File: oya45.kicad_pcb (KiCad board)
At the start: 2 copper layers, 94 parts, among them U1 Elite-C

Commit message: added pro micro
pro micro instead of elite c for less pads
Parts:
- U1: value Elite-C -> ProMicro; footprint Keebio-Parts:Elite-C -> Keebio-Parts:ArduinoProMicro
- moved U1 1.59 mm to (218.3, 38.1)
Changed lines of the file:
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@@
     (zones 0)
     (modules 94)
-    (nets 75)
+    (nets 70)
   )
   (page A4)
@@
   (net 68 "Net-(U1-Pad2)")
   (net 69 "Net-(U1-Pad1)")
-  (net 70 "Net-(U1-Pad25)")
-  (net 71 "Net-(U1-Pad26)")
-  (net 72 "Net-(U1-Pad27)")
-  (net 73 "Net-(U1-Pad28)")
-  (net 74 "Net-(U1-Pad29)")
   (net_class Default "This is the default net class."
     (clearance 0.00508)
@@
     (add_net "Net-(U1-Pad23)")
     (add_net "Net-(U1-Pad24)")
-    (add_net "Net-(U1-Pad25)")
-    (add_net "Net-(U1-Pad26)")
-    (add_net "Net-(U1-Pad27)")
-    (add_net "Net-(U1-Pad28)")
-    (add_net "Net-(U1-Pad29)")
     (add_net "Net-(U1-Pad3)")
     (add_net "Net-(U1-Pad4)")
@@
     (add_net row4)
   )
-  (module Keebio-Parts:Elite-C (layer F.Cu)
-    (at 219.86875 38.1 180)
+  (module Keebio-Parts:ArduinoProMicro (layer F.Cu)
+    (at 218.28125 38.1 180)
     (fp_text reference U1 (at 0 1.625) (layer F.SilkS) hide
-      (effects (font (size 1.2 1.2) (thickness 0.2032)))
-    )
-    (fp_text value Elite-C (at 0 0) (layer F.SilkS) hide
-      (effects (font (size 1.2 1.2) (thickness 0.2032)))
-    )
-    (fp_text user D5 (at 12.4 2.54 90) (layer B.SilkS)
-      (effects (font (size 0.8 0.8) (thickness 0.15)) (justify mirror))
-    )
-    (fp_text user D5 (at 12.4 2.54 90) (layer F.SilkS)
-      (effects (font (size 0.8 0.8) (thickness 0.15)))
-    )
-    (fp_text user F1 (at 12.4 -2.54 90) (layer F.SilkS)
-      (effects (font (size 0.8 0.8) (thickness 0.15)))
-    )
-    (fp_text user F1 (at 12.4 -2.54 90) (layer B.SilkS)
-      (effects (font (size 0.8 0.8) (thickness 0.15)) (justify mirror))
-    )
-    (fp_text user C7 (at 12.4 0 90) (layer B.SilkS)
-      (effects (font (size 0.8 0.8) (thickness 0.15)) (justify mirror))
-    )
-    (fp_text user C7 (at 12.4 0 90) (layer F.SilkS)
-      (effects (font (size 0.8 0.8) (thickness 0.15)))
-    )
-    (fp_text user B6 (at 12.7 -6.4 315 unlocked) (layer B.SilkS)
-      (effects (font (size 0.7 0.7) (thickness 0.15)) (justify mirror))
-    )
-    (fp_text user B6 (at 12.7 -6.4 315 unlocked) (layer F.SilkS)
-      (effects (font (size 0.7 0.7) (thickness 0.15)))
-    )
-    (fp_text user F0 (at 12.6 -4.5 90) (layer F.SilkS)
-      (effects (font (size 0.7 0.7) (thickness 0.15)))
-    )
-    (fp_text user F0 (at 12.6 -4.5 90) (layer B.SilkS)
-      (effects (font (size 0.7 0.7) (thickness 0.15)) (justify mirror))
-    )
-    (fp_text user B7 (at 12.6 4.5 90) (layer B.SilkS)
-      (effects (font (size 0.7 0.7) (thickness 0.15)) (justify mirror))
-    )
-    (fp_text user B7 (at 12.6 4.5 90) (layer F.SilkS)
-      (effects (font (size 0.7 0.7) (thickness 0.15)))
+      (effects (font (size 1.27 1.524) (thickness 0.2032)))
+    )
+    (fp_text value ProMicro (at 0 0) (layer F.SilkS) hide
+      (effects (font (size 1.27 1.524) (thickness 0.2032)))
     )
     (fp_line (start -15.24 6.35) (end -15.24 8.89) (layer F.SilkS) (width 0.381))
@@
       (effects (font (size 0.8 0.8) (thickness 0.15)))
     )
-    (fp_text user B5 (at 12.7 6.4 45) (layer F.SilkS)
-      (effects (font (size 0.7 0.7) (thickness 0.15)))
+    (fp_text user B5 (at 13.97 5.461 90) (layer F.SilkS)
+      (effects (font (size 0.8 0.8) (thickness 0.15)))
+    )
+    (fp_text user B6 (at 13.97 -5.461 90) (layer F.SilkS)
+      (effects (font (size 0.8 0.8) (thickness 0.15)))
     )
     (fp_text user B2 (at 11.43 -5.461 90) (layer B.SilkS)
@@
       (effects (font (size 0.8 0.8) (thickness 0.15)))
     )
-    (fp_text user B0 (at -13.97 -5.461 90) (layer F.SilkS)
-      (effects (font (size 0.8 0.8) (thickness 0.15)))
-    )
-    (fp_text user B0 (at -13.97 -5.461 90) (layer B.SilkS)
+    (fp_text user RAW (at -13.97 -5.461 90) (layer F.SilkS)
+      (effects (font (size 0.8 0.8) (thickness 0.15)))
+    )
+    (fp_text user RAW (at -13.97 -5.461 90) (layer B.SilkS)
       (effects (font (size 0.8 0.8) (thickness 0.15)) (justify mirror))
     )
@@
       (effects (font (size 0.8 0.8) (thickness 0.15)))
     )
-    (fp_text user B5 (at 12.7 6.4 45) (layer B.SilkS)
-      (effects (font (size 0.7 0.7) (thickness 0.15)) (justify mirror))
+    (fp_text user B6 (at 13.97 -5.461 90) (layer B.SilkS)
+      (effects (font (size 0.8 0.8) (thickness 0.15)) (justify mirror))
+    )
+    (fp_text user B5 (at 13.97 5.461 90) (layer B.SilkS)
+      (effects (font (size 0.8 0.8) (thickness 0.15)) (justify mirror))
     )
     (fp_text user B4 (at 11.43 5.461 90) (layer B.SilkS)
@@
     (fp_line (start -15.24 6.35) (end -12.7 6.35) (layer B.SilkS) (width 0.381))
     (fp_line (start -12.7 6.35) (end -12.7 8.89) (layer B.SilkS) (width 0.381))
-    (pad 25 thru_hole circle (at 13.97 5.08 180) (size 1.7526 1.7526) (drill 1.0922) (layers *.Cu *.SilkS *.Mask)
-      (net 70 "Net-(U1-Pad25)"))
-    (pad 26 thru_hole circle (at 13.97 2.54 180) (size 1.7526 1.7526) (drill 1.0922) (layers *.Cu *.SilkS *.Mask)
-      (net 71 "Net-(U1-Pad26)"))
-    (pad 27 thru_hole circle (at 13.97 0 180) (size 1.7526 1.7526) (drill 1.0922) (layers *.Cu *.SilkS *.Mask)
-      (net 72 "Net-(U1-Pad27)"))
-    (pad 28 thru_hole circle (at 13.97 -2.54 180) (size 1.7526 1.7526) (drill 1.0922) (layers *.Cu *.SilkS *.Mask)
-      (net 73 "Net-(U1-Pad28)"))
-    (pad 29 thru_hole circle (at 13.97 -5.08 180) (size 1.7526 1.7526) (drill 1.0922) (layers *.Cu *.SilkS *.Mask)
-      (net 74 "Net-(U1-Pad29)"))
     (pad 24 thru_hole circle (at -13.97 -7.62 180) (size 1.7526 1.7526) (drill 1.0922) (layers *.Cu *.SilkS *.Mask)
       (net 61 "Net-(U1-Pad24)"))
-    (pad 12 thru_hole circle (at 13.97 7.3914 180) (size 1.7526 1.7526) (drill 1.0922) (layers *.Cu *.SilkS *.Mask)
+    (pad 12 thru_hole circle (at 13.97 7.62 180) (size 1.7526 1.7526) (drill 1.0922) (layers *.Cu *.SilkS *.Mask)
       (net 53 col2))
     (pad 23 thru_hole circle (at -11.43 -7.62 180) (size 1.7526 1.7526) (drill 1.0922) (layers *.Cu *.SilkS *.Mask)

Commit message: added fillets
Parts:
- moved U1 43.9 mm to (208.8, -4.76)
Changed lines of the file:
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@@
   (general
     (thickness 1.6)
-    (drawings 0)
+    (drawings 6)
     (tracks 0)
     (zones 0)
@@
   )
   (module Keebio-Parts:ArduinoProMicro (layer F.Cu)
-    (at 218.28125 38.1 180)
+    (at 208.75625 -4.7625 180)
     (fp_text reference U1 (at 0 1.625) (layer F.SilkS) hide
       (effects (font (size 1.27 1.524) (thickness 0.2032)))
@@
       (net 1 row1))
   )
+  (gr_arc (start 150.01875 30.95625) (end 152.4 30.95625) (angle -90) (layer F.SilkS) (width 0.12))
+  (gr_arc (start 235.74375 50.00625) (end 238.125 50.00625) (angle -90) (layer F.SilkS) (width 0.12))
+  (gr_arc (start 235.74375 121.44375) (end 235.74375 123.825) (angle -90) (layer F.SilkS) (width 0.12))
+  (gr_arc (start 50.00625 121.44375) (end 47.625 121.44375) (angle -90) (layer F.SilkS) (width 0.12))
+  (gr_arc (start 50.00625 50.00625) (end 50.00625 47.625) (angle -90) (layer F.SilkS) (width 0.12))
+  (gr_arc (start 59.53125 30.95625) (end 59.53125 28.575) (angle -90) (layer F.SilkS) (width 0.12))
 )

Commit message: column tracing
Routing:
- net col4: track 0.00 -> 100.1 mm
- net col3: track 0.00 -> 80.1 mm
- net col2: track 0.00 -> 80.1 mm
- net col1: track 0.00 -> 80.1 mm
- net col5: track 0.00 -> 66.7 mm
- net col0: track 0.00 -> 61.1 mm
- net col6: track 0.00 -> 58.1 mm
- net col9: track 0.00 -> 57.2 mm
- net col8: track 0.00 -> 57.2 mm
- net col7: track 0.00 -> 57.2 mm
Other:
- net class Default: clearance 0.00508 -> 0.2; trace_width 0.00508 -> 0.254
- rule trace_clearance: 0.00508 -> 0.2
- rule trace_min: 0.00381 -> 0.2
- rule via_min_drill: 0.00762 -> 0.3
- rule via_min_size: 0.00381 -> 0.4
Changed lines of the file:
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@@
     (thickness 1.6)
     (drawings 6)
-    (tracks 0)
+    (tracks 31)
     (zones 0)
     (modules 94)
@@
   )
   (setup
-    (last_trace_width 0.00508)
-    (trace_clearance 0.00508)
+    (last_trace_width 0.254)
+    (trace_clearance 0.2)
     (zone_clearance 0.508)
     (zone_45_only no)
-    (trace_min 0.00381)
+    (trace_min 0.2)
     (via_size 0.8)
     (via_drill 0.4)
-    (via_min_size 0.00381)
-    (via_min_drill 0.00762)
+    (via_min_size 0.4)
+    (via_min_drill 0.3)
     (uvia_size 0.3)
     (uvia_drill 0.1)
     (uvias_allowed no)
-    (uvia_min_size 0.00381)
-    (uvia_min_drill 0.00254)
+    (uvia_min_size 0.2)
+    (uvia_min_drill 0.1)
     (edge_width 0.05)
     (segment_width 0.2)
@@
   (net 69 "Net-(U1-Pad1)")
   (net_class Default "This is the default net class."
-    (clearance 0.00508)
-    (trace_width 0.00508)
+    (clearance 0.2)
+    (trace_width 0.254)
     (via_dia 0.8)
     (via_drill 0.4)
@@
   (gr_arc (start 50.00625 50.00625) (end 50.00625 47.625) (angle -90) (layer F.SilkS) (width 0.12))
   (gr_arc (start 59.53125 30.95625) (end 59.53125 28.575) (angle -90) (layer F.SilkS) (width 0.12))
+  (segment (start 70.485 45.085) (end 60.96 54.61) (width 0.254) (layer F.Cu) (net 51))
+  (segment (start 70.485 35.56) (end 70.485 45.085) (width 0.254) (layer F.Cu) (net 51))
+  (segment (start 60.96 54.61) (end 60.96 92.71) (width 0.254) (layer F.Cu) (net 51))
+  (segment (start 89.535 45.085) (end 80.01 54.61) (width 0.254) (layer F.Cu) (net 52))
+  (segment (start 89.535 35.56) (end 89.535 45.085) (width 0.254) (layer F.Cu) (net 52))
+  (segment (start 80.01 54.61) (end 80.01 111.76) (width 0.254) (layer F.Cu) (net 52))
+  (segment (start 108.585 45.085) (end 99.06 54.61) (width 0.254) (layer F.Cu) (net 53))
+  (segment (start 108.585 35.56) (end 108.585 45.085) (width 0.254) (layer F.Cu) (net 53))
+  (segment (start 99.06 54.61) (end 99.06 111.76) (width 0.254) (layer F.Cu) (net 53))
+  (segment (start 127.635 45.085) (end 118.11 54.61) (width 0.254) (layer F.Cu) (net 54))
+  (segment (start 127.635 35.56) (end 127.635 45.085) (width 0.254) (layer F.Cu) (net 54))
+  (segment (start 118.11 54.61) (end 118.11 111.76) (width 0.254) (layer F.Cu) (net 54))
+  (segment (start 146.685 45.085) (end 137.16 54.61) (width 0.254) (layer F.Cu) (net 55))
+  (segment (start 146.685 35.56) (end 146.685 45.085) (width 0.254) (layer F.Cu) (net 55))
+  (segment (start 137.16 54.61) (end 137.16 103.02875) (width 0.254) (layer F.Cu) (net 55))
+  (segment (start 138.284999 110.635001) (end 137.16 111.76) (width 0.254) (layer F.Cu) (net 55))
+  (segment (start 138.284999 104.153749) (end 138.284999 110.635001) (width 0.254) (layer F.Cu) (net 55))
+  (segment (start 137.16 103.02875) (end 138.284999 104.153749) (width 0.254) (layer F.Cu) (net 55))
+  (segment (start 138.75099 111.76) (end 146.685 111.76) (width 0.254) (layer B.Cu) (net 55))
+  (segment (start 137.16 111.76) (end 138.75099 111.76) (width 0.254) (layer B.Cu) (net 55))
+  (segment (start 137.16 111.76) (end 127.635 111.76) (width 0.254) (layer B.Cu) (net 55))
+  (segment (start 156.21 54.61) (end 156.21 111.76) (width 0.254) (layer F.Cu) (net 56))
+  (segment (start 157.80099 111.76) (end 165.735 111.76) (width 0.254) (layer F.Cu) (net 56))
+  (segment (start 156.21 111.76) (end 157.80099 111.76) (width 0.254) (layer F.Cu) (net 56))
+  (segment (start 175.26 54.61) (end 175.26 103.02875) (width 0.254) (layer F.Cu) (net 57))
+  (segment (start 176.384999 110.635001) (end 175.26 111.76) (width 0.254) (layer F.Cu) (net 57))
+  (segment (start 176.384999 104.153749) (end 176.384999 110.635001) (width 0.254) (layer F.Cu) (net 57))
+  (segment (start 175.26 103.02875) (end 176.384999 104.153749) (width 0.254) (layer F.Cu) (net 57))
+  (segment (start 194.31 54.61) (end 194.31 111.76) (width 0.254) (layer F.Cu) (net 58))
+  (segment (start 213.36 54.61) (end 213.36 111.76) (width 0.254) (layer F.Cu) (net 59))
+  (segment (start 232.41 54.61) (end 232.41 111.76) (width 0.254) (layer F.Cu) (net 60))
 )

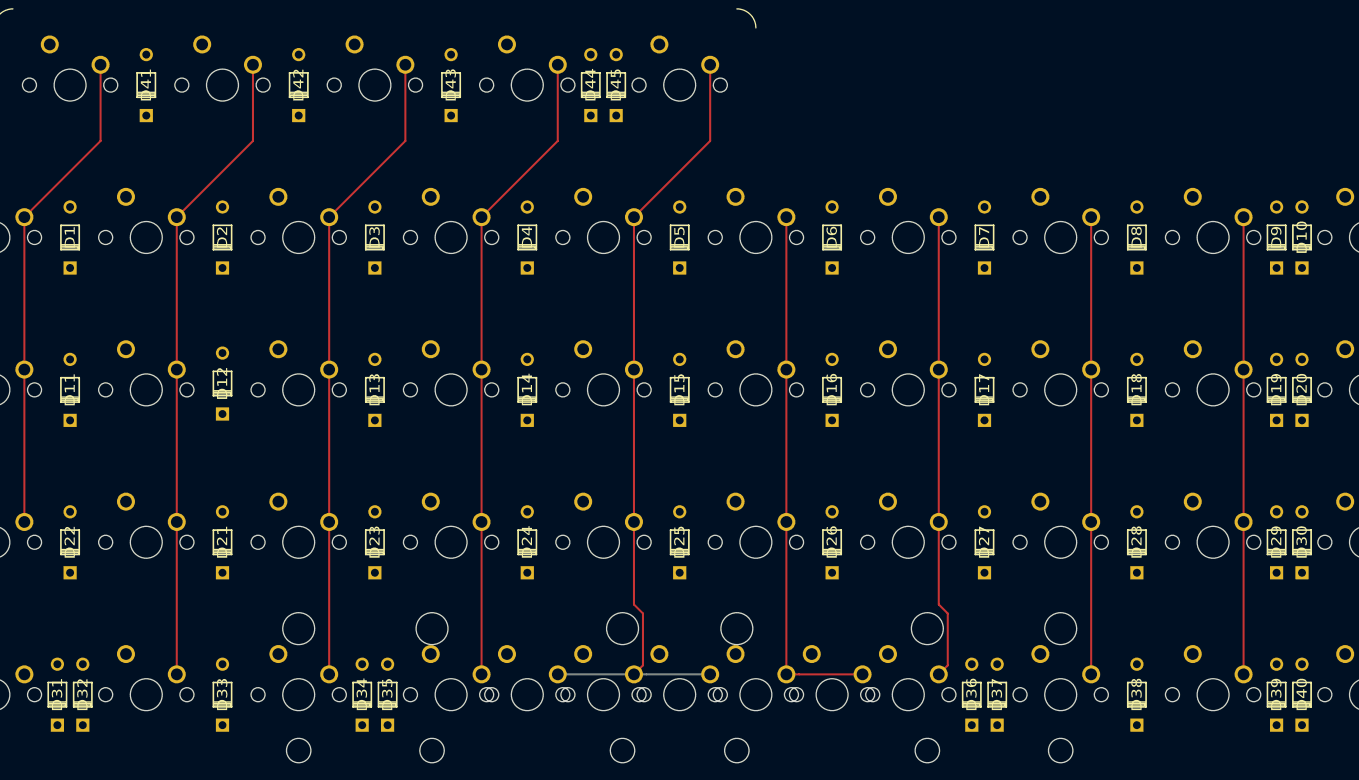
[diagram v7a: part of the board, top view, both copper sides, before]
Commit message: diode orientation fix
flipped the diodes because they were facing in a less convenient way
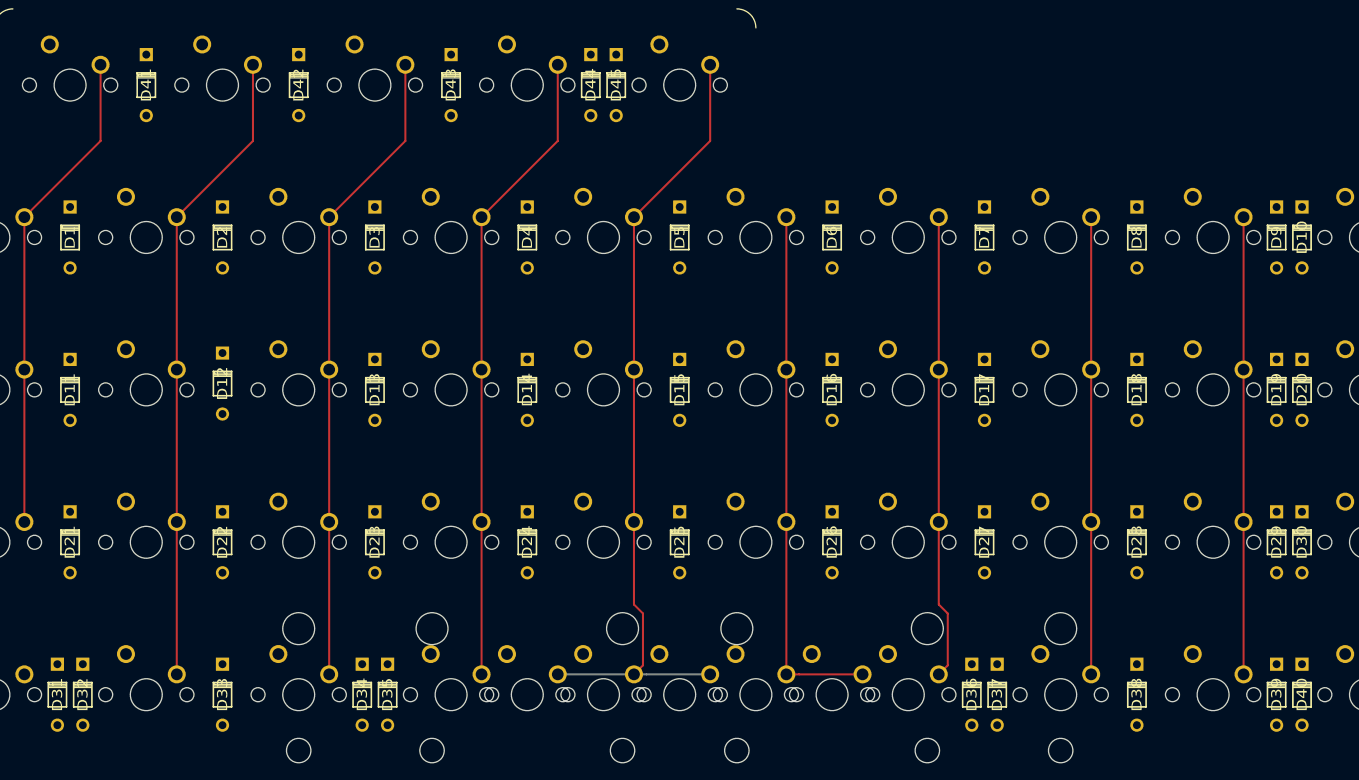
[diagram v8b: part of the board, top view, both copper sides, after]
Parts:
- moved D21 19.0 mm to (66.7, 95.2), turned to 90 degrees
- moved D22 19.0 mm to (85.7, 95.2), turned to 90 degrees
- turned D1 to 90 degrees
- turned D10 to 90 degrees
- turned D11 to 90 degrees
- turned D12 to 90 degrees
- turned D13 to 90 degrees
- turned D14 to 90 degrees
- turned D15 to 90 degrees
- turned D16 to 90 degrees
- turned D17 to 90 degrees
- turned D18 to 90 degrees
- turned D19 to 90 degrees
- turned D2 to 90 degrees
- turned D20 to 90 degrees
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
